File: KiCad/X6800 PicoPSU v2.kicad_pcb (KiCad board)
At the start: 2 copper layers, 179.8 x 93.8 mm, 15 parts

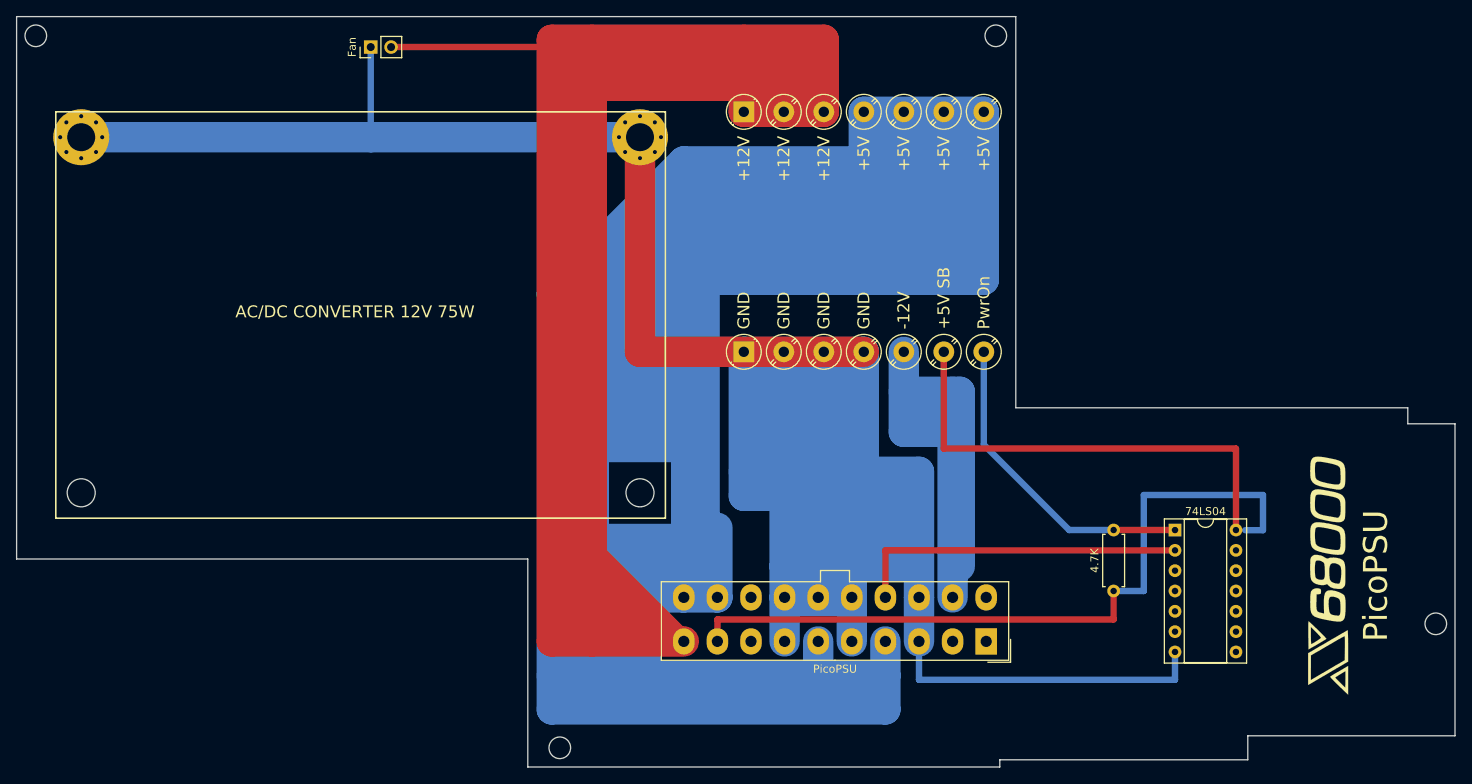
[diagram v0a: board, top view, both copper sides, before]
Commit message: Cyo Commit
-Add QR code on PCB to github link
-Add more documentation and instructions for assembly.
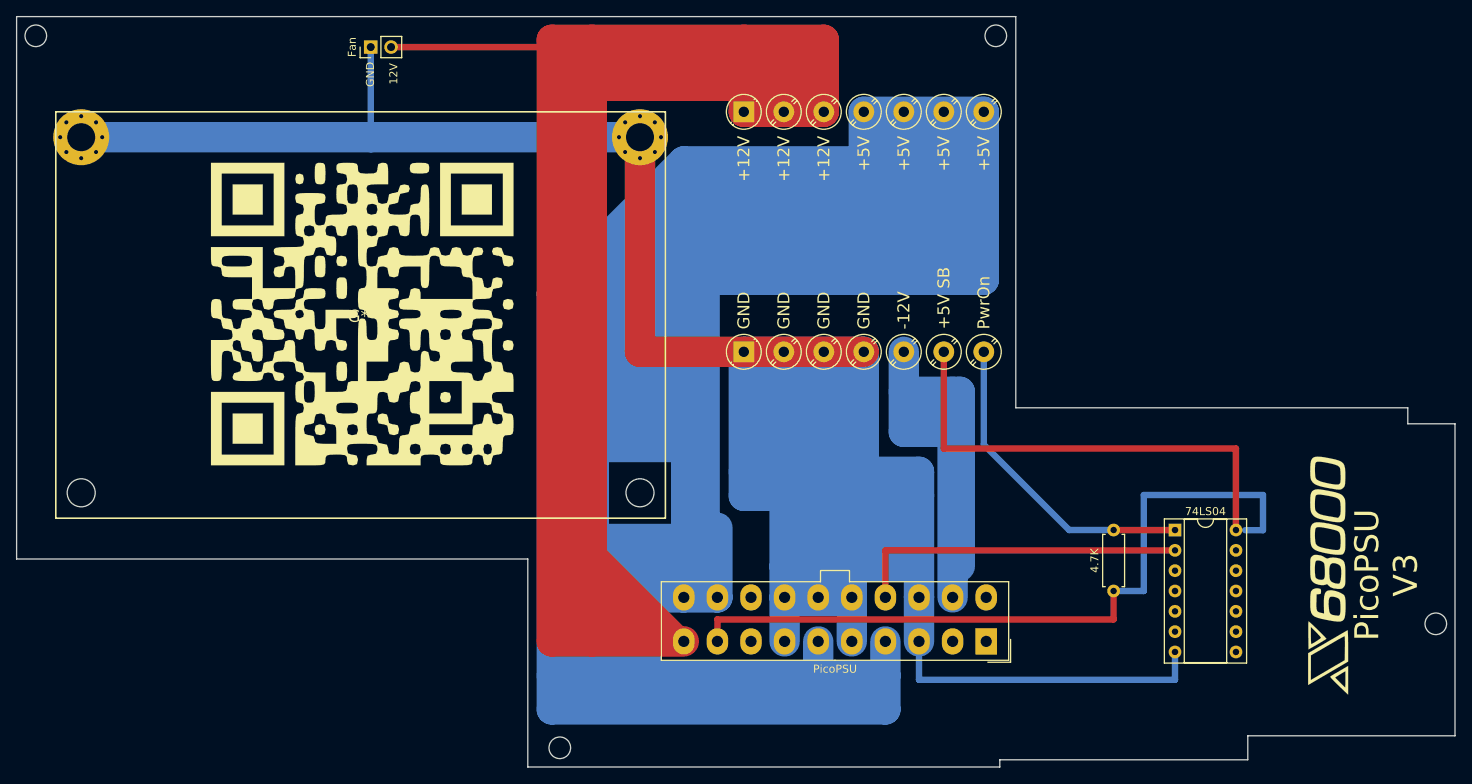
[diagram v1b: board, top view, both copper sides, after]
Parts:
- added G***: LOGO, KiCad:QR_CODE, F.Cu at (99.8, 87.6)
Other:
- net class Default removed
- board text added: "12V"
- board text added: "PicoPSU V3"
- board text removed: "AC/DC CONVERTER 12V 75W"
- board text removed: "PicoPSU"
